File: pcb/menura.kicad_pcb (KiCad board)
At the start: 2 copper layers, 123 x 97.2 mm, 56 parts

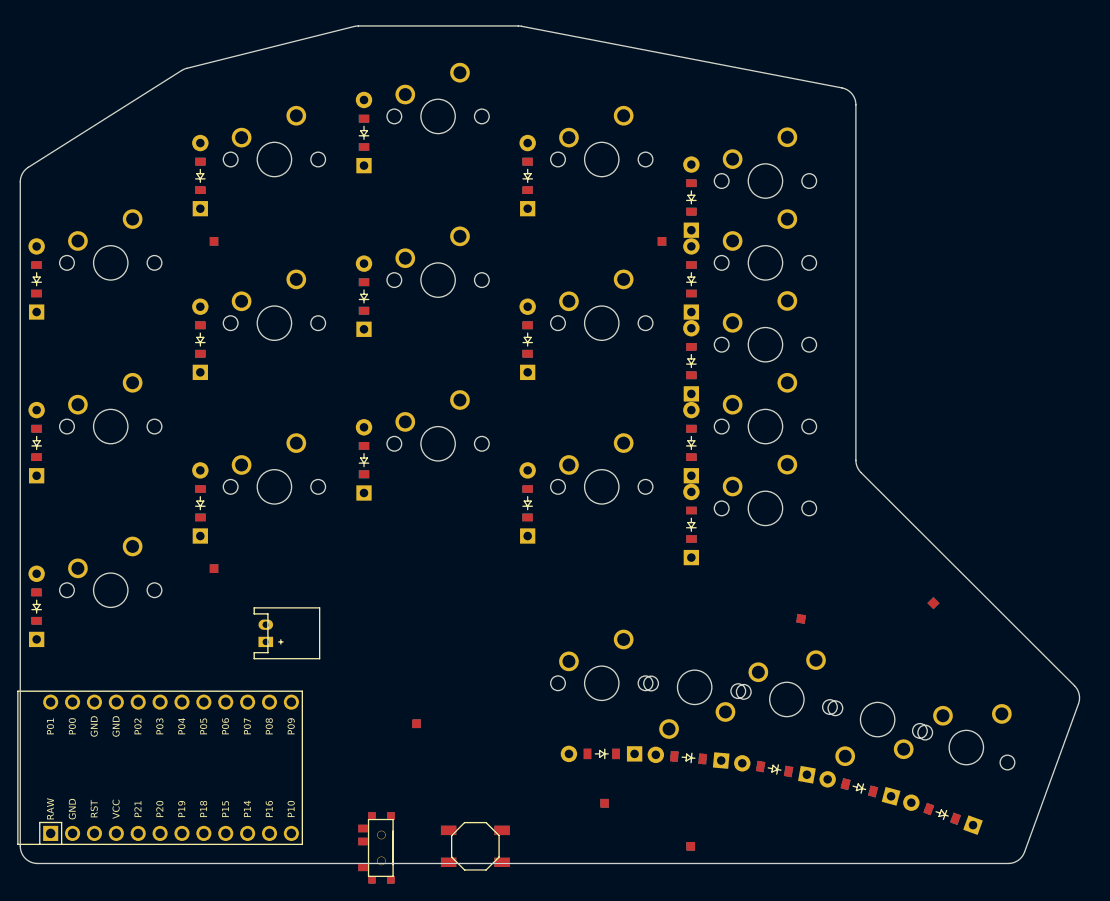
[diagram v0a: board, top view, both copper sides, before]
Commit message: reorder a few pins
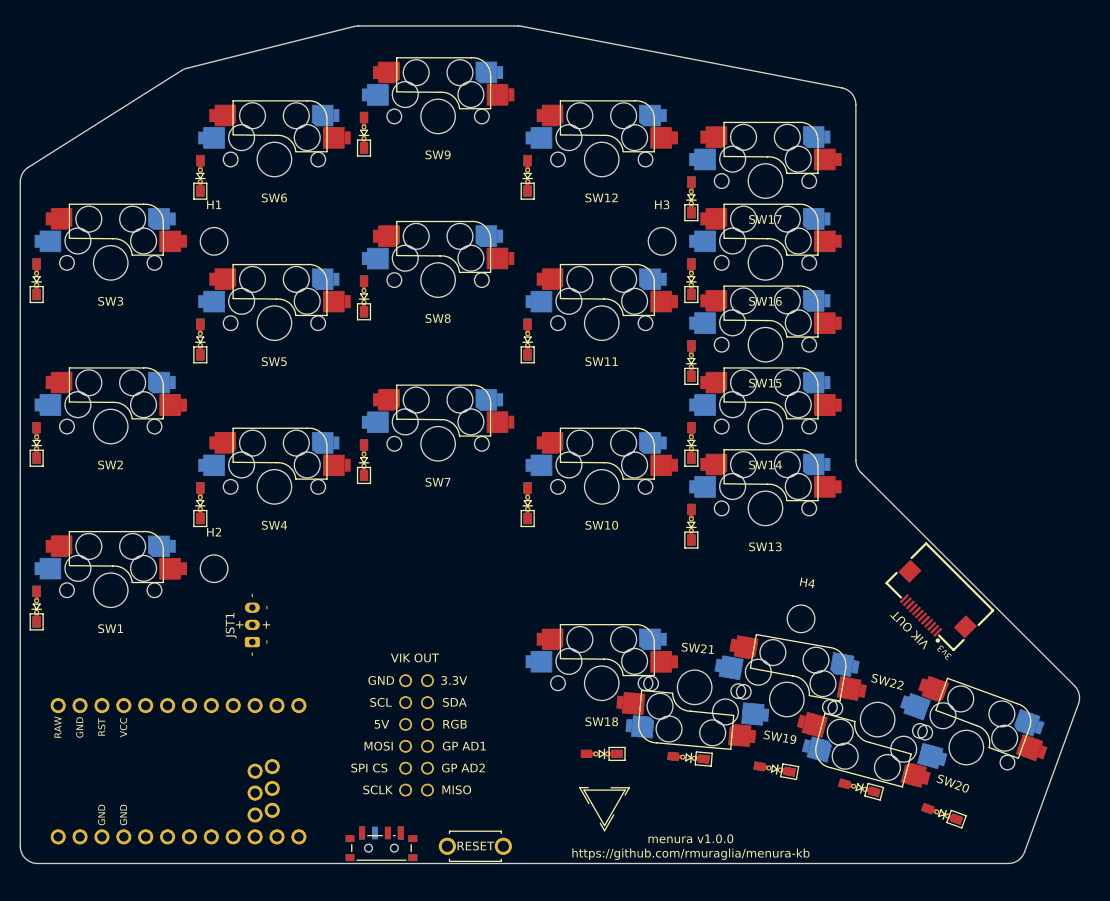
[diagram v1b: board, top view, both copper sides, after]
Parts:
- D1, D10, D11, D12, D13, D14, D15, D16, D17, D18, D19, D2, D20, D21, D22, D3, D4, D5, D6, D7, D8, D9: value (none) -> 1N4148W; footprint ComboDiode -> quappo:Diode_SMD-reversible-urchin
- H1, H2, H3, H4: value (none) -> MountingHole; footprint SMDPad -> MountingHole:MountingHole_3.2mm_M3
- JST1: value (none) -> Conn_01x03_Socket; footprint JST_PH_S2B-PH-K_02x2.00mm_Angled -> quappo:Connector_JST-PH-3prong
- LOGO1: value (none) -> menura; footprint SMDPad -> quappo:Logo_menura
- LOGO2: value (none) -> vik; footprint SMDPad -> quappo:Logo_vik-small
- MCU1: value (none) -> N!N; footprint ProMicro -> quappo:MCU_nice-nano
- PWR1: value (none) -> SW_SPDT; footprint E73:SPDT_C128955 -> quappo:Switch_power-reversible-kim
- RSW1: value (none) -> SW_Push; footprint E73:SW_TACT_ALPS_SKQGABE010 -> quappo:Switch_reset-2pin
- SW1, SW10, SW11, SW12, SW13, SW14, SW15, SW16, SW17, SW18, SW19, SW2, SW20, SW21, SW22, SW3, SW4, SW5, SW6, SW7, SW8, SW9: value (none) -> SW_Push; footprint MX -> quappo:Switch_MX-hotswap-reversible
- VIK1: value (none) -> ~; footprint SMDPad -> quappo:Connector_vik-keyboard-horizontal
- VIK2: value (none) -> ~; footprint SMDPad -> quappo:Connector_vik-keyboard-throughhole
- moved JST1 1.35 mm to (118.9, 104.0)
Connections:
- D1 pad 1: (no net) -> row2
- D1 pad 2: (no net) -> Net-(D1-A)
- D10 pad 1: (no net) -> row2
- D10 pad 2: (no net) -> Net-(D10-A)
- D11 pad 1: (no net) -> row1
- D11 pad 2: (no net) -> Net-(D11-A)
- D12 pad 1: (no net) -> row0
- D12 pad 2: (no net) -> Net-(D12-A)
- D13 pad 1: (no net) -> row2
- D13 pad 2: (no net) -> Net-(D13-A)
- D14 pad 1: (no net) -> row1
- D14 pad 2: (no net) -> Net-(D14-A)
- D15 pad 1: (no net) -> row1
- D15 pad 2: (no net) -> Net-(D15-A)
- D16 pad 1: (no net) -> row0
- D16 pad 2: (no net) -> Net-(D16-A)
- D17 pad 1: (no net) -> row0
- D17 pad 2: (no net) -> Net-(D17-A)
- D18 pad 1: (no net) -> row3
- D18 pad 2: (no net) -> Net-(D18-A)
- D19 pad 1: (no net) -> row3
- D19 pad 2: (no net) -> Net-(D19-A)
- D2 pad 1: (no net) -> row1
- D2 pad 2: (no net) -> Net-(D2-A)
- D20 pad 1: (no net) -> row3
- D20 pad 2: (no net) -> Net-(D20-A)
- D21 pad 1: (no net) -> row3
- D21 pad 2: (no net) -> Net-(D21-A)
- D22 pad 1: (no net) -> row3
- D22 pad 2: (no net) -> Net-(D22-A)
- D3 pad 1: (no net) -> row0
- D3 pad 2: (no net) -> Net-(D3-A)
- D4 pad 1: (no net) -> row2
- D4 pad 2: (no net) -> Net-(D4-A)
- D5 pad 1: (no net) -> row1
- D5 pad 2: (no net) -> Net-(D5-A)
- D6 pad 1: (no net) -> row0
- D6 pad 2: (no net) -> Net-(D6-A)
- D7 pad 1: (no net) -> row2
- D7 pad 2: (no net) -> Net-(D7-A)
- D8 pad 1: (no net) -> row1
- D8 pad 2: (no net) -> Net-(D8-A)
- D9 pad 1: (no net) -> row0
- D9 pad 2: (no net) -> Net-(D9-A)
- JST1 pad 1: (no net) -> GND
- JST1 pad 2: (no net) -> Net-(JST1-Pin_2)
- MCU1 pad 1: RAW -> row0
- MCU1 pad 10: P14 -> SCLK
- MCU1 pad 11: P16 -> unconnected-(MCU1-104-Pad11)
- MCU1 pad 12: P10 -> row3
- MCU1 pad 13: P1 -> col4
- MCU1 pad 14: P0 -> col3
- MCU1 pad 15: GND -> col2
- MCU1 pad 16: GND -> col1
- MCU1 pad 17: P2 -> VIK_GPIO2
- MCU1 pad 18: P3 -> VIK_GPIO1
- MCU1 pad 19: P4 -> col0
- MCU1 pad 2: GND -> row1
- MCU1 pad 20: P5 -> row2
- MCU1 pad 21: P6 -> +3.3V
- MCU1 pad 22: P7 -> RST
- MCU1 pad 23: P8 -> GND
- MCU1 pad 24: P9 -> RAW
- MCU1 pad 3: RST -> GND
- MCU1 pad 4: VCC -> GND
- MCU1 pad 5: P21 -> SCL
- MCU1 pad 6: P20 -> SDA
- MCU1 pad 7: P19 -> MOSI
- MCU1 pad 8: P18 -> CS
- MCU1 pad 9: P15 -> MISO
- PWR1 pad 1: (no net) -> RAW
- PWR1 pad 2: (no net) -> Net-(JST1-Pin_2)
- PWR1 pad 3: (no net) -> unconnected-(PWR1-C-Pad3)
- RSW1 pad 1: (no net) -> GND
- RSW1 pad 2: (no net) -> RST
- SW1 pad 1: (no net) -> col0
- SW1 pad 2: (no net) -> Net-(D1-A)
- SW10 pad 1: (no net) -> col3
- SW10 pad 2: (no net) -> Net-(D10-A)
- SW11 pad 1: (no net) -> col3
- SW11 pad 2: (no net) -> Net-(D11-A)
- SW12 pad 1: (no net) -> col3
- SW12 pad 2: (no net) -> Net-(D12-A)
- SW13 pad 1: (no net) -> col4
- SW13 pad 2: (no net) -> Net-(D13-A)
- SW14 pad 1: (no net) -> col4
- SW14 pad 2: (no net) -> Net-(D14-A)
- SW15 pad 1: (no net) -> col4
- SW15 pad 2: (no net) -> Net-(D15-A)
- SW16 pad 1: (no net) -> col4
- SW16 pad 2: (no net) -> Net-(D16-A)
- SW17 pad 1: (no net) -> col4
- SW17 pad 2: (no net) -> Net-(D17-A)
- SW18 pad 1: (no net) -> col2
- SW18 pad 2: (no net) -> Net-(D18-A)
- SW19 pad 1: (no net) -> col3
- SW19 pad 2: (no net) -> Net-(D19-A)
- SW2 pad 1: (no net) -> col0
- SW2 pad 2: (no net) -> Net-(D2-A)
- SW20 pad 1: (no net) -> col4
- SW20 pad 2: (no net) -> Net-(D20-A)
- SW21 pad 1: (no net) -> col2
- SW21 pad 2: (no net) -> Net-(D21-A)
- SW22 pad 1: (no net) -> col3
- SW22 pad 2: (no net) -> Net-(D22-A)
- SW3 pad 1: (no net) -> col0
- SW3 pad 2: (no net) -> Net-(D3-A)
- SW4 pad 1: (no net) -> col1
- SW4 pad 2: (no net) -> Net-(D4-A)
- SW5 pad 1: (no net) -> col1
- SW5 pad 2: (no net) -> Net-(D5-A)
- SW6 pad 1: (no net) -> col1
- SW6 pad 2: (no net) -> Net-(D6-A)
- SW7 pad 1: (no net) -> col2
- SW7 pad 2: (no net) -> Net-(D7-A)
- SW8 pad 1: (no net) -> col2
- SW8 pad 2: (no net) -> Net-(D8-A)
- SW9 pad 1: (no net) -> col2
- SW9 pad 2: (no net) -> Net-(D9-A)
- VIK1 pad 1: (no net) -> +3.3V
- VIK2 pad 1: (no net) -> +3.3V
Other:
- net class Default removed

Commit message: bird silhouette logo
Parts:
- removed LOGO2: vik, quappo:Logo_vik-small
- LOGO1: value menura -> menura_composite; footprint quappo:Logo_menura -> quappo:Logo_menura_composite
- moved LOGO1 3.50 mm to (167.3, 126.2)

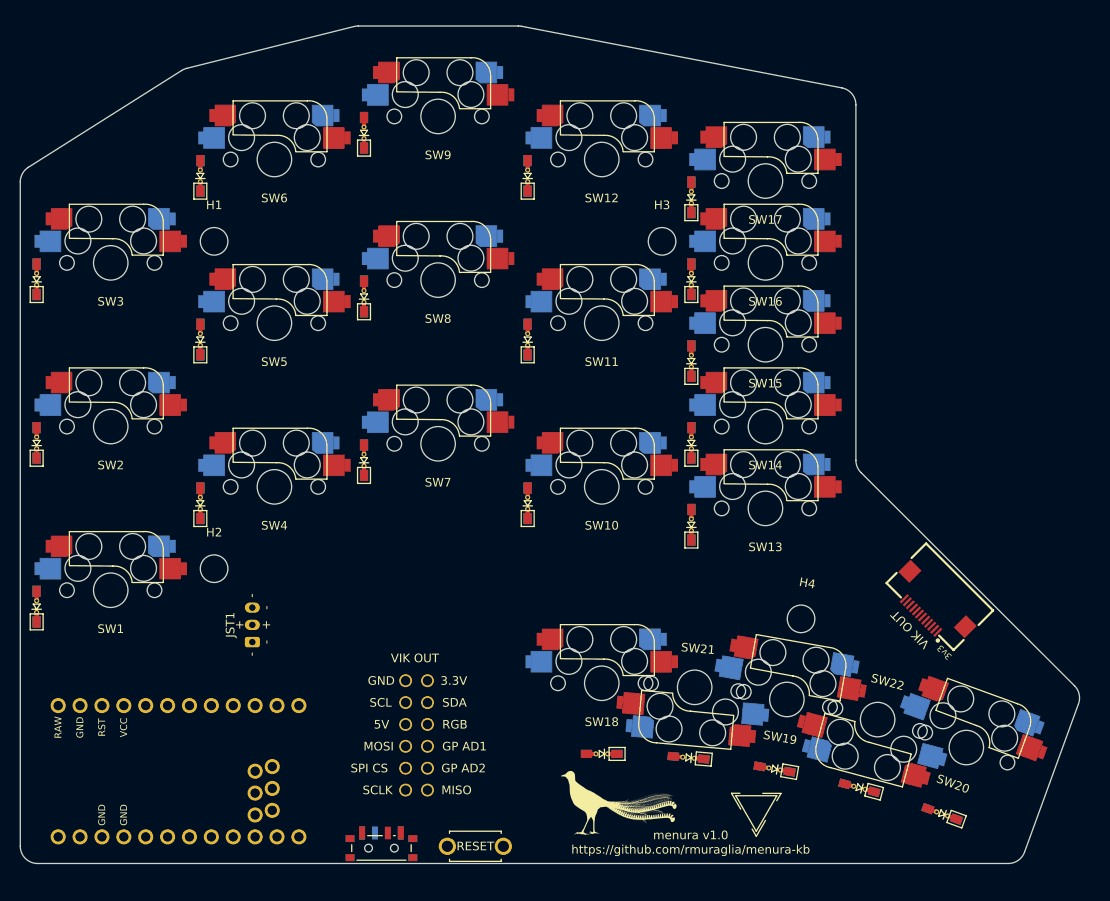
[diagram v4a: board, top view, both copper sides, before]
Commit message: routing partially done
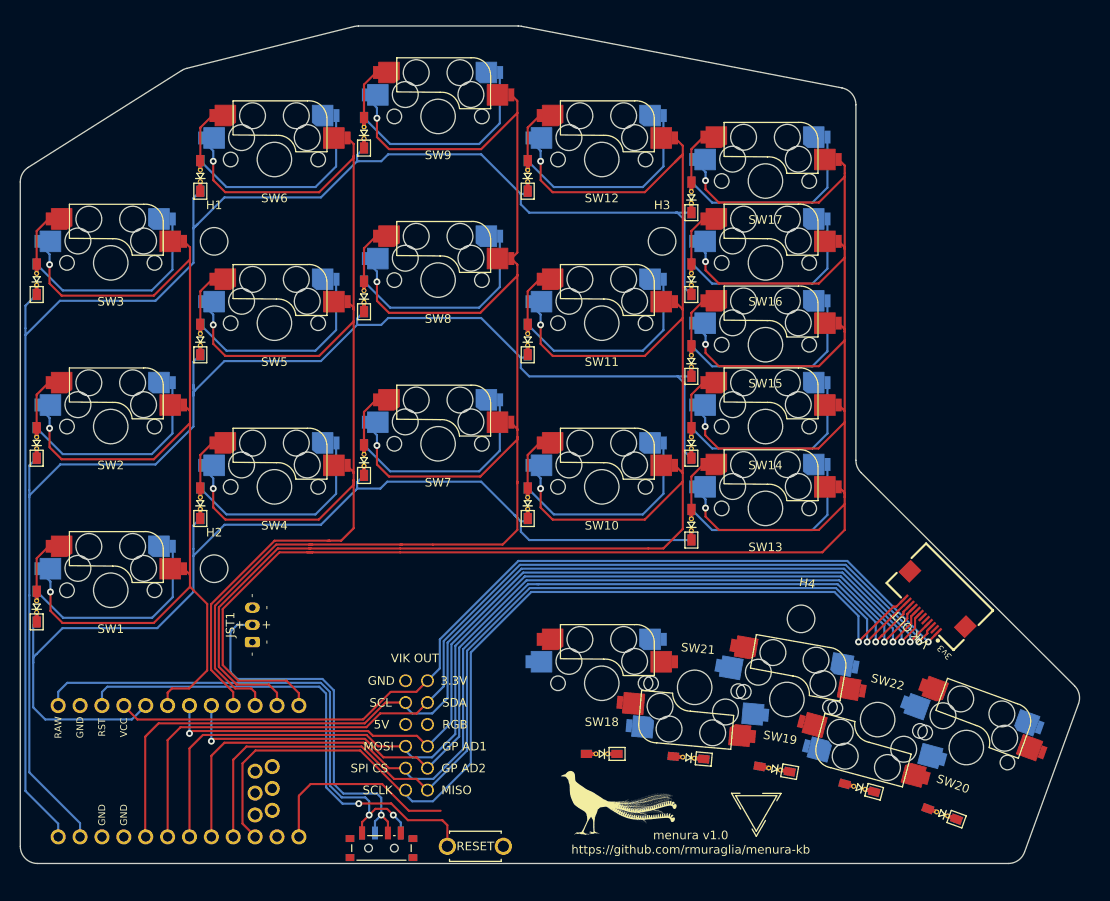
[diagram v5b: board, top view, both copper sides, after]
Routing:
- net col4: track 0.00 -> 253.9 mm, vias 0 -> 5
- net col3: track 0.00 -> 196.8 mm, vias 0 -> 3
- net col2: track 0.00 -> 179.7 mm, vias 0 -> 3
- net row0: track 0.00 -> 175.1 mm
- net row1: track 0.00 -> 156.4 mm
- net col1: track 0.00 -> 154.2 mm, vias 0 -> 3
- net col0: track 0.00 -> 134.0 mm, vias 0 -> 3
- net row2: track 0.00 -> 123.8 mm
- net SCL: track 0.00 -> 120.7 mm, vias 0 -> 1
- net MOSI: track 0.00 -> 117.4 mm, vias 0 -> 1
- net SDA: track 0.00 -> 116.4 mm, vias 0 -> 1
- net CS: track 0.00 -> 115.6 mm, vias 0 -> 1
- net SCLK: track 0.00 -> 113.2 mm, vias 0 -> 1
- net MISO: track 0.00 -> 112.5 mm, vias 0 -> 1
- net +3.3V: track 0.00 -> 109.1 mm, vias 0 -> 1
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
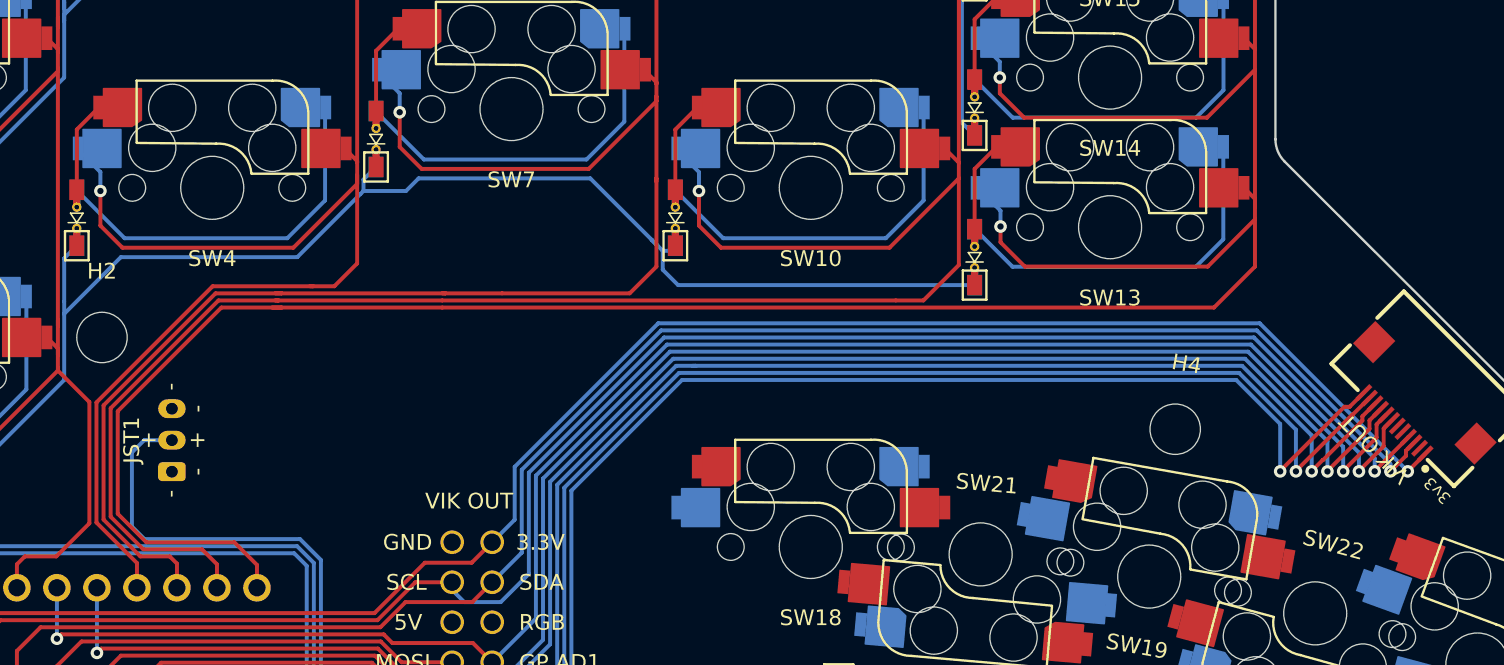
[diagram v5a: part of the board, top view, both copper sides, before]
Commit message: column crossovers
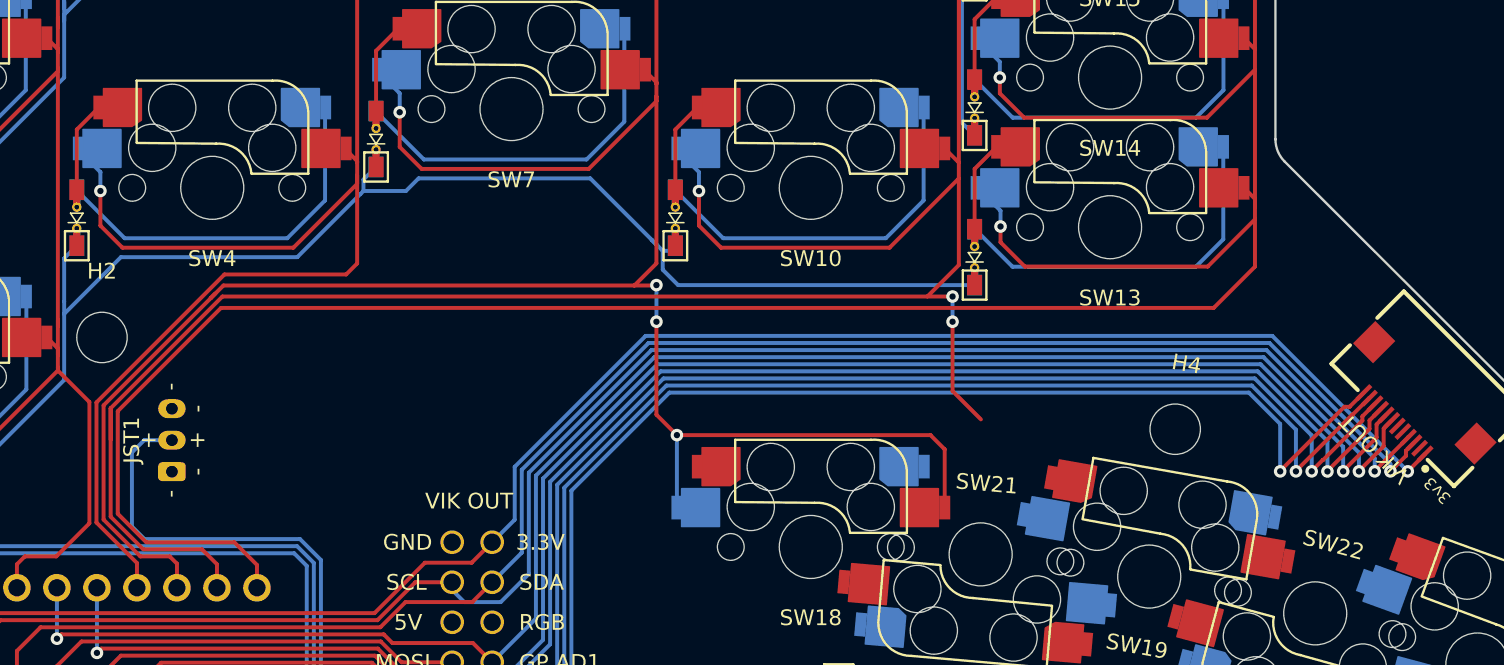
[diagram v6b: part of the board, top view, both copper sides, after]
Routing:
- net col2: track 179.7 -> 216.3 mm, vias 3 -> 6
- net col3: track 196.8 -> 208.7 mm, vias 3 -> 5
- net CS: track 115.6 -> 114.7 mm
- net +3.3V: track 109.1 -> 108.4 mm
- net VIK_GPIO2: track 108.3 -> 107.6 mm
- net SDA: track 116.4 -> 115.8 mm
- net SCLK: track 113.2 -> 112.5 mm
- net MISO: track 112.5 -> 111.9 mm
- net SCL: track 120.7 -> 120.0 mm
- net MOSI: track 117.4 -> 116.8 mm
- net VIK_GPIO1: track 108.5 -> 107.9 mm
- net col4: track 253.9 -> 253.3 mm
